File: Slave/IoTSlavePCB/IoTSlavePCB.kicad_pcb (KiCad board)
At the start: 4 copper layers, 44.2 x 41.5 mm, 48 parts, among them J1 M50-3610742R, J2 10118194-0001LF, J3 Conn_01x02, U1 STM32L412RBT6P, U2 MCP73831T-2ACI/OT, U3 MYRGP180100B21RA, U4 MYRGP100100B21RA, U5 SHTC3, U6 AT86RF232-ZX, U7 IS25WQ040-JNLE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

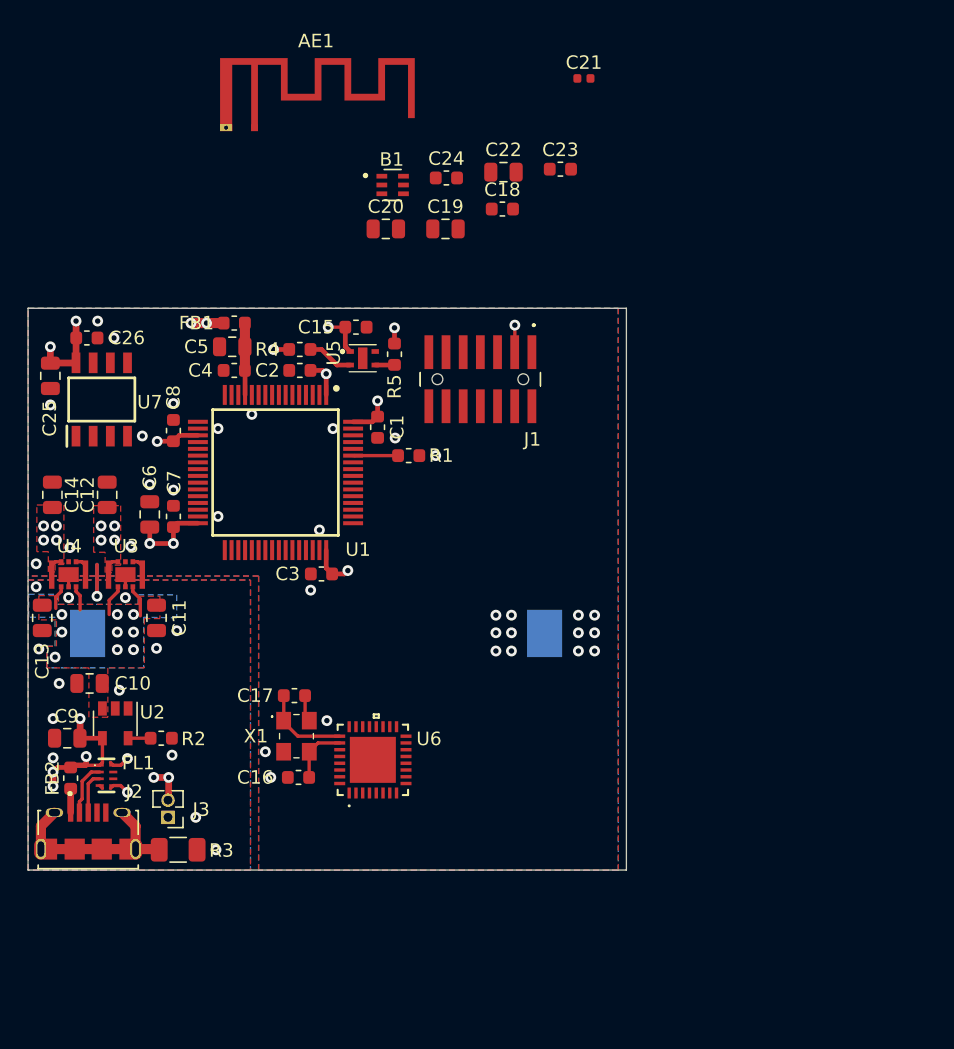
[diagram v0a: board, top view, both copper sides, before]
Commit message: Made more connections on PCB, some optimizations. Added silk screen text.
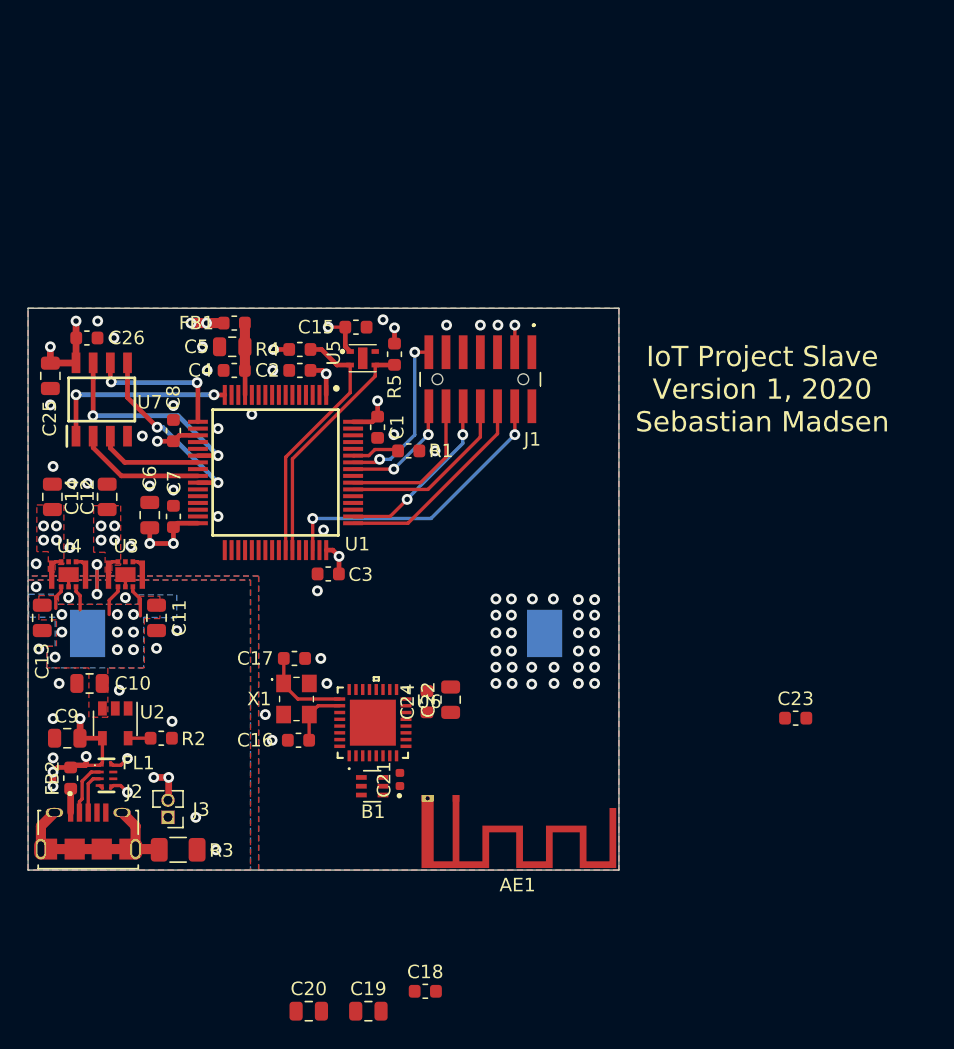
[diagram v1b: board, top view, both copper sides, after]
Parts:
- AE1: footprint RF_Antenna:Texas_SWRA117D_2.4GHz_Right -> RF_Antenna:Texas_SWRA117D_2.4GHz_Left
- moved C18 58.1 mm to (163.0, 132.1)
- moved C19 58.1 mm to (158.8, 133.5)
- moved C20 58.1 mm to (154.4, 133.5)
- moved C21 53.6 mm to (161.1, 116.4), turned to 90 degrees
- moved AE1 51.8 mm to (165.2, 117.8), turned to 180 degrees
- moved B1 44.5 mm to (159.1, 116.9), turned to 180 degrees
- moved C23 44.2 mm to (190.4, 111.9)
- moved C22 39.2 mm to (164.8, 110.5), turned to 90 degrees
- moved C24 38.8 mm to (163.1, 110.7), turned to 90 degrees
- moved C16 2.75 mm to (153.6, 113.5)
- moved C17 2.75 mm to (153.3, 107.5)
- moved U6 2.75 mm to (159.1, 112.2)
- moved X1 2.75 mm to (153.4, 110.5)
- moved C3 0.50 mm to (155.8, 101.2)
- moved R1 0.35 mm to (161.8, 92.1)
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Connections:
- net /MCU/USB_DM renamed /MCU/USB_DN
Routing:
- net /MCU/JTMS: track 0.00 -> 22.0 mm, vias 0 -> 2
- net /MCU/I2C1_SDA: track 1.43 -> 17.7 mm
- net /Memory/QSPI_DATA3: track 0.00 -> 15.9 mm, vias 0 -> 2
- net /MCU/I2C1_SCL: track 3.41 -> 19.1 mm
- net /MCU/JTCK: track 0.00 -> 15.5 mm
- net /MCU/QSPI_NCS: track 0.00 -> 14.1 mm, vias 0 -> 2
- net /Memory/QSPI_DATA0: track 0.00 -> 13.4 mm, vias 0 -> 2
- net /MCU/JTDO: track 0.00 -> 13.3 mm
- net /MCU/JTDI: track 0.00 -> 13.1 mm, vias 0 -> 2
- net /MCU/USART_RX: track 0.00 -> 12.6 mm, vias 0 -> 2
- net /MCU/NRST: track 0.00 -> 11.4 mm
- net /MCU/QSPI_CLK: track 0.00 -> 10.7 mm, vias 0 -> 2
- net /Memory/QSPI_DATA1: track 0.00 -> 9.46 mm
- net /MCU/USART_TX: track 0.00 -> 8.73 mm, vias 0 -> 2
- net /Memory/QSPI_DATA2: track 0.00 -> 7.79 mm
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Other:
- board size 44.2 x 41.5 mm -> 43.7 x 41.5 mm
- net class USB added: clearance 0.2, trace_width 0.25, via_dia 0.8, via_drill 0.4
- board text added: "IoT Project Slave Version 1, 2020 Sebastian Madsen"

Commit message: Everything placed. Only needs final routes and optimization.
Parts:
- removed C23: 100 nF, Capacitor_SMD:C_0603_1608Metric
- moved C20 20.8 mm to (166.2, 116.5)
- moved C18 19.4 mm to (153.6, 115.0)
- moved C19 17.6 mm to (153.4, 116.8)
- moved B1 2.07 mm to (160.2, 118.7), turned to 270 degrees
- moved C21 1.01 mm to (162.1, 116.2), turned to 0 degrees
- moved AE1 0.08 mm to (165.2, 117.7)
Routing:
- net +1V8: track 35.4 -> 50.2 mm, vias 18 -> 22
- net GND: track 9.58 -> 23.4 mm, vias 78 -> 97
- net Net-(AE1-Pad1): track 0.00 -> 6.56 mm
- net Net-(B1-Pad4): track 0.00 -> 5.07 mm
- net Net-(B1-Pad3): track 0.00 -> 3.26 mm
- net Net-(B1-Pad2): track 0.00 -> 2.57 mm

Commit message: Further PCB work.
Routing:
- net /MCU/~RF_RST: track 0.00 -> 38.2 mm, vias 0 -> 2
- net /MCU/RF_SLP_TR: track 0.00 -> 29.7 mm, vias 0 -> 2
- net /MCU/USB_DP: track 0.00 -> 28.7 mm, vias 0 -> 2
- net /ZigBee/IRQ: track 0.00 -> 28.7 mm, vias 0 -> 4
- net /MCU/SPI2_MISO: track 0.00 -> 27.8 mm, vias 0 -> 2
- net /MCU/USB_DN: track 0.00 -> 27.5 mm, vias 0 -> 2
- net /MCU/SPI2_MOSI: track 0.00 -> 27.0 mm, vias 0 -> 2
- net /MCU/SPI2_SCK: track 0.00 -> 24.0 mm, vias 0 -> 2
- net /MCU/~SPI2_NSS: track 0.00 -> 16.0 mm
- net GND: track 23.4 -> 23.5 mm, vias 97 -> 99

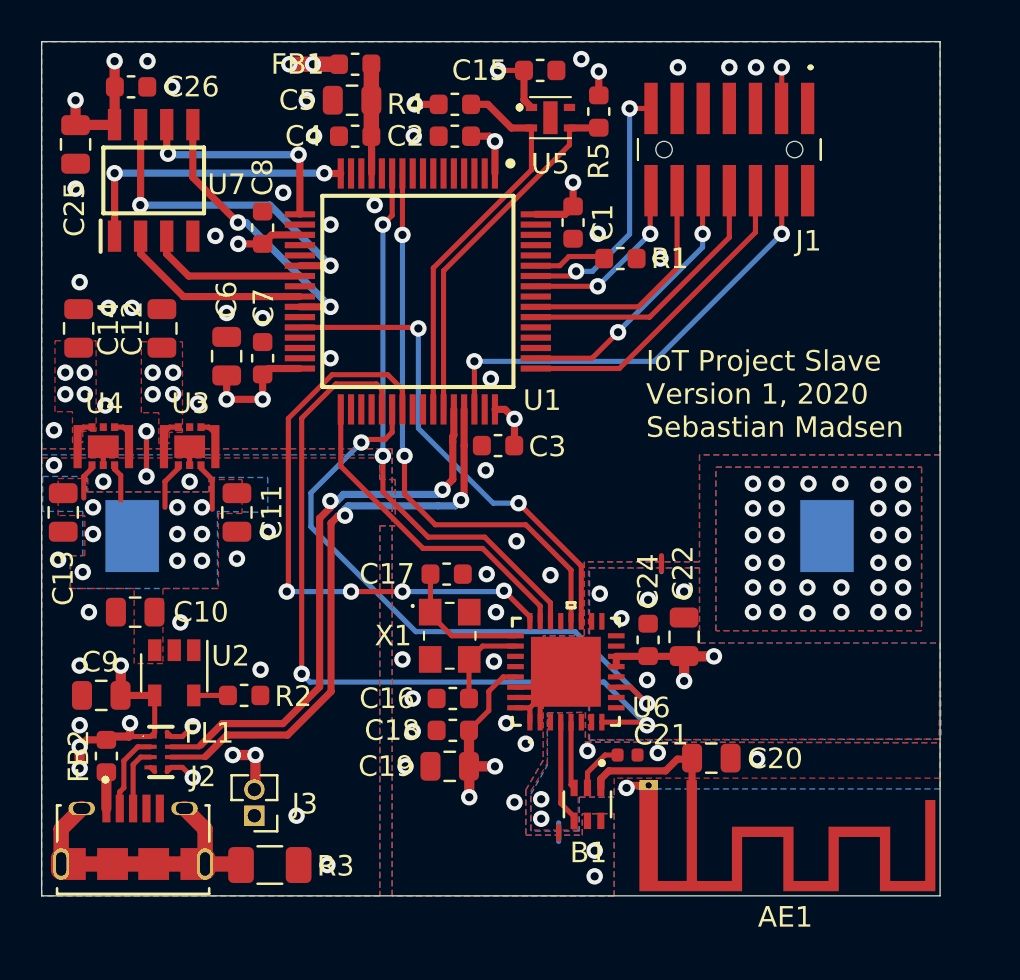
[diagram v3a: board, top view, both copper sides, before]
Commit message: Prettified PCB, some changes to routes and planes for performance.
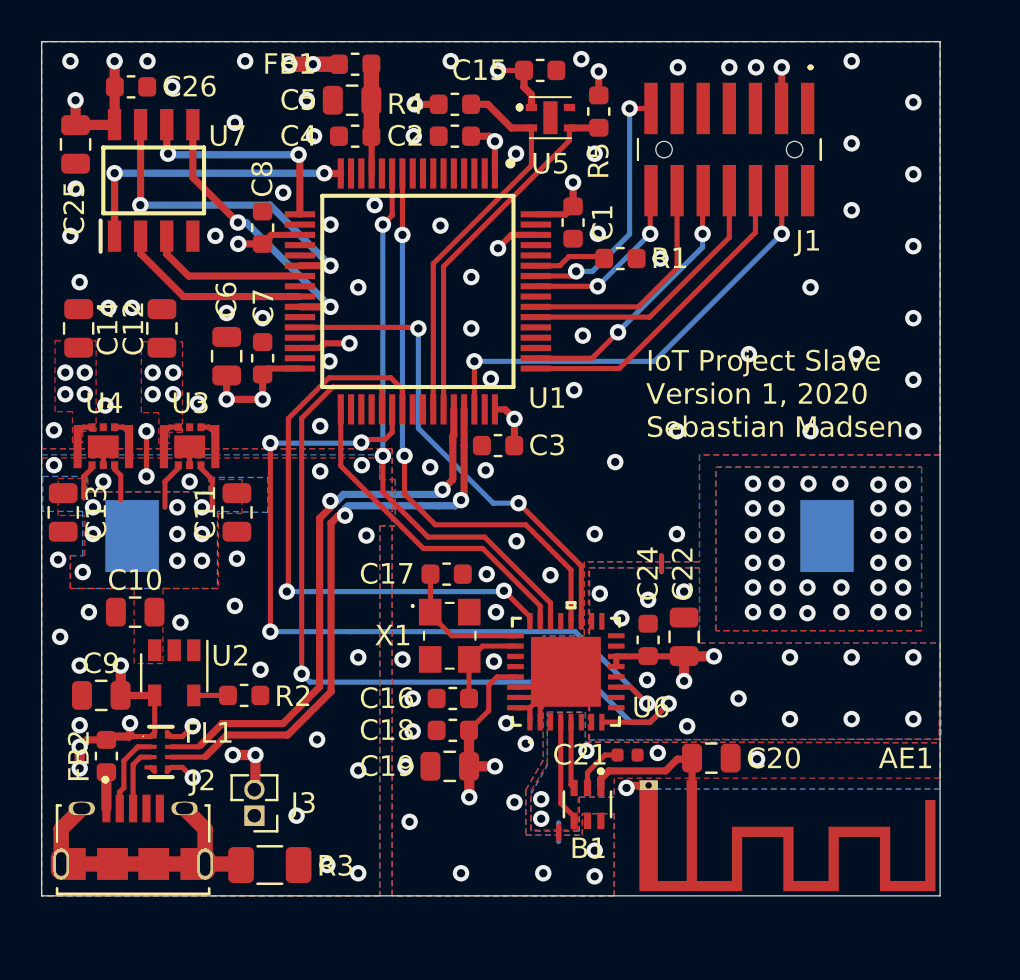
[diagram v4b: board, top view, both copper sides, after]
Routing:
- net +1V0: track 1.49 -> 28.7 mm, vias 4 -> 6
- net /MCU/RF_SLP_TR: track 29.7 -> 38.0 mm, vias 2 -> 4
- net /MCU/~RF_RST: track 38.2 -> 40.8 mm
- net /ZigBee/IRQ: track 28.7 -> 28.6 mm, vias 4 -> 2
- net GND: vias 99 -> 150

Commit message: Change for clarity.
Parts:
- BT1: footprint Personal_Misc:SMTU2430-LF -> Personal_Misc:SMTU2450-LF

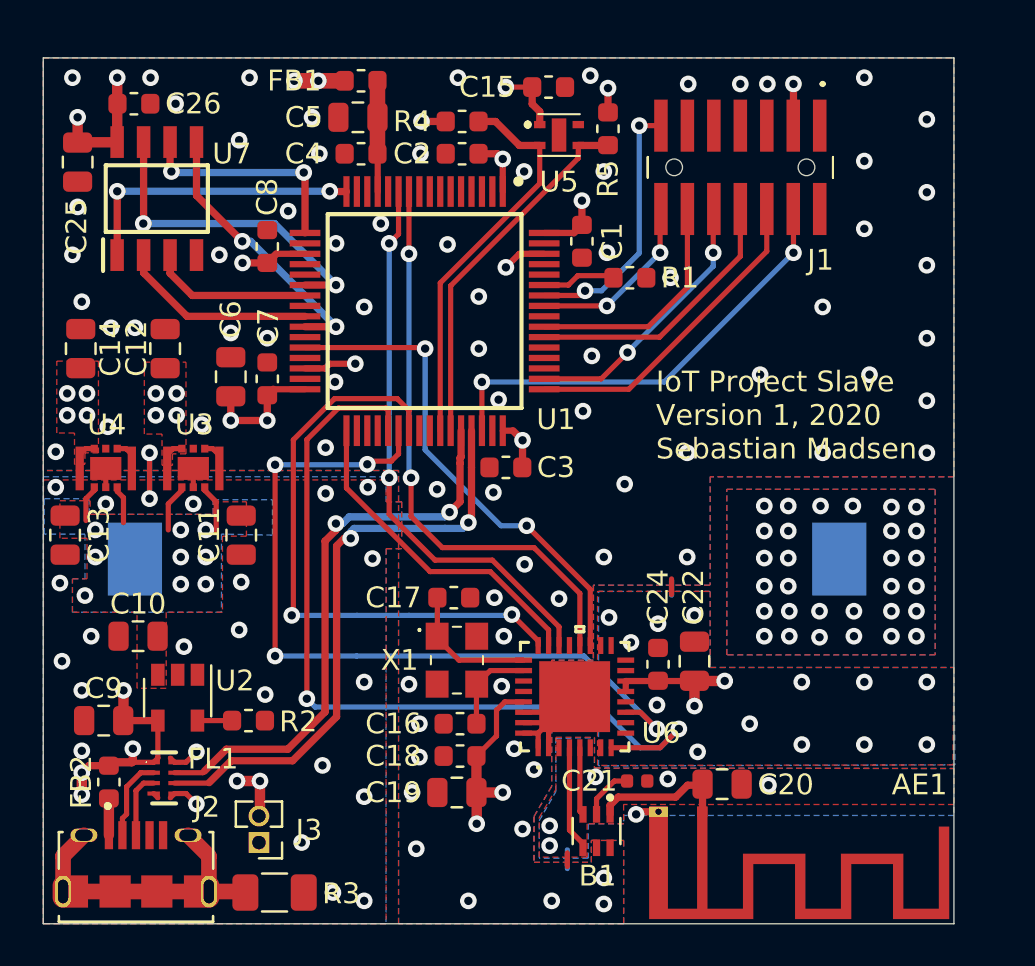
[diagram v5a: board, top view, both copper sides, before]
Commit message: Added battery voltage measurement circuit. Optimizations to antenna and general component placement.
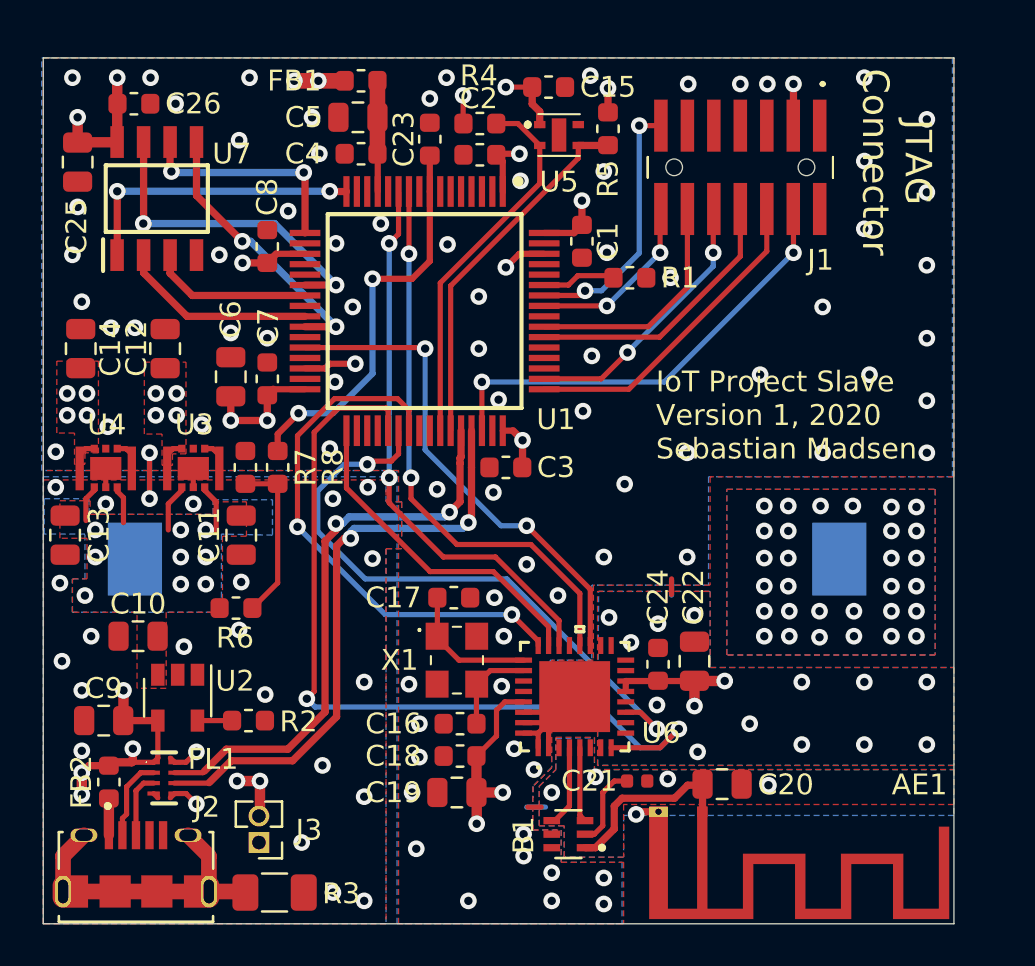
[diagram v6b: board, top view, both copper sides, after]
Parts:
- added C23: 100 nF, Capacitor_SMD:C_0603_1608Metric, F.Cu at (152.2, 85.5)
- added R6: 10M, Resistor_SMD:R_0603_1608Metric, F.Cu at (142.8, 108.0)
- added R7: 4.99M, Resistor_SMD:R_0603_1608Metric, F.Cu at (143.3, 101.2)
- added R8: 10k, Resistor_SMD:R_0603_1608Metric, F.Cu at (144.8, 101.2)
- moved B1 1.36 mm to (158.8, 118.8), turned to 180 degrees
- moved R4 0.86 mm to (154.6, 84.7)
- moved C2 0.85 mm to (154.6, 86.2)
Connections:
- U1 pad 8: Net-(U1-Pad8) -> /MCU/ADC_Battery
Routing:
- net /MCU/ADC_Battery: track 0.00 -> 19.3 mm, vias 0 -> 2
- net /MCU/RF_SLP_TR: track 38.0 -> 29.7 mm, vias 4 -> 2
- net Net-(R6-Pad1): track 0.00 -> 8.01 mm
- net /ZigBee/IRQ: track 28.6 -> 25.7 mm
- net Net-(AE1-Pad1): track 6.56 -> 8.88 mm
- net Net-(B1-Pad2): track 2.57 -> 4.00 mm
- net Net-(B1-Pad4): track 5.07 -> 3.94 mm
- net /MCU/I2C1_SCL: track 19.1 -> 18.2 mm
- net GND: vias 150 -> 151
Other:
- board text added: "JTAG Connector"
